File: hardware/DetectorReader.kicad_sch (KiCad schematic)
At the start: 17 parts, among them J1 10118194-0001LF, J2 Combo_Conn, J3 SMA_Conn, SW1 SeqTrig_SW, U1 ATtiny814-SS, U2 FT231XS-R, U3 XC0900P-10S

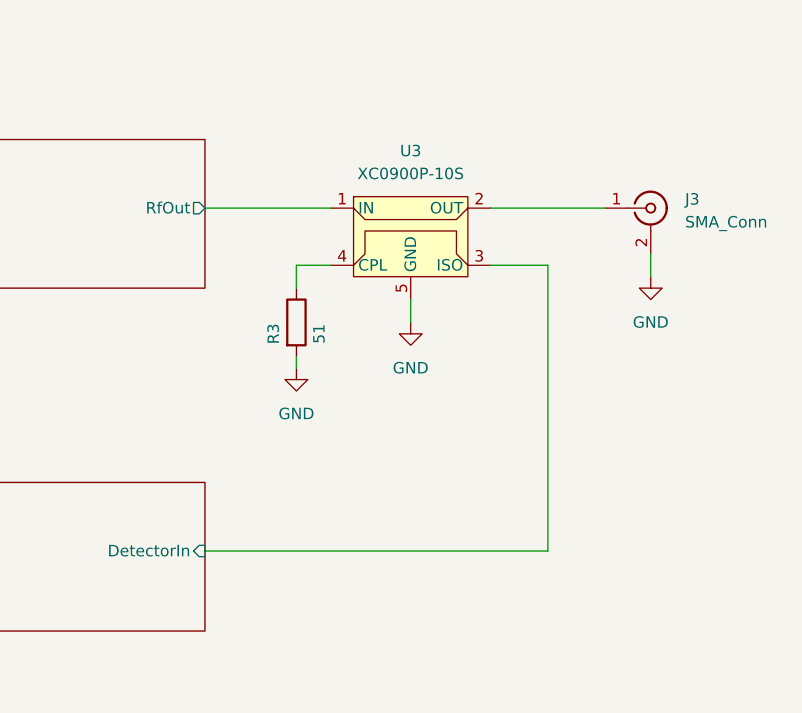
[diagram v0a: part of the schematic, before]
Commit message: added PA and changed directional coupler
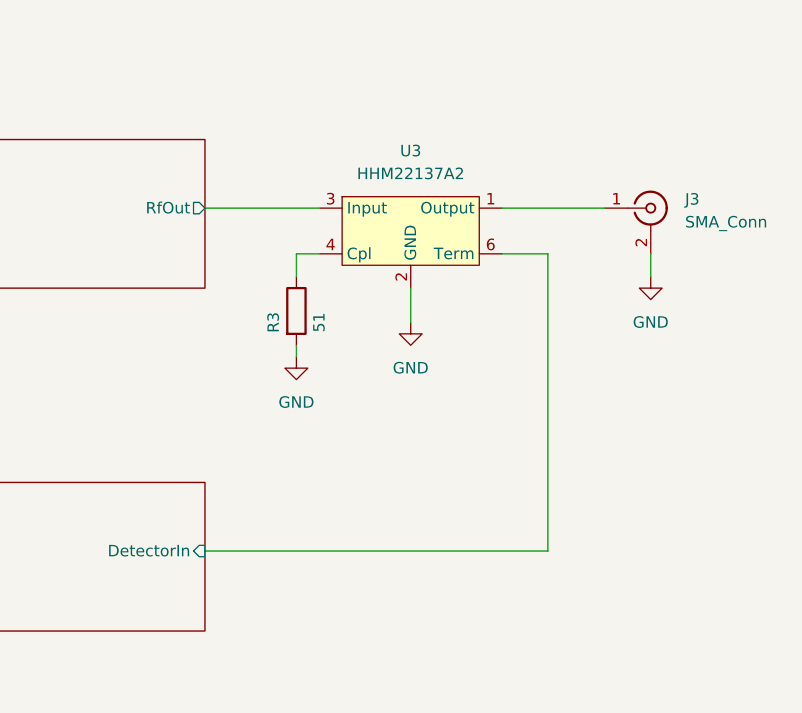
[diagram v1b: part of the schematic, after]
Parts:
- removed U3: XC0900P-10S, ProjLib:Xinger2, symbol ProjLib:XC0900P-10S
- added U3: HHM22137A2, ProjLib:EIA0603, symbol ProjLib:HHM22137A2
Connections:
- net GND: now also U3.2 (GND), U3.5 (GND)
- net RF_Rx/DetectorIn: now also U3.6 (Term)
- net RF_Tx/RfOut: now also U3.3 (Input)
- net at J3.1 (In): now also U3.1 (Output)
- net at R3.1: now also U3.4 (Cpl)
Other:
- moved on the sheet: R3
